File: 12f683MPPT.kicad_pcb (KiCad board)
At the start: 2 copper layers, 97.8 x 72.6 mm, 58 parts, among them J1(+) Conn_01x01_Male, J2(-) Conn_01x01_Male, J3(-) Conn_01x01_Male, J4(+) Conn_01x01_Male, J5(Vin) Vin, J6(GND) GND, J7(12V) 12V, Q1(BUK9511-55A) BUK9511-55A127, Q2(BUK9511-55A) BUK9511-55A127, Q3(2N2222A) 2N2222A, Q4(2N2222A) 2N2222A, Q5(2N2907A) 2N2907A, SW1 SW_Push

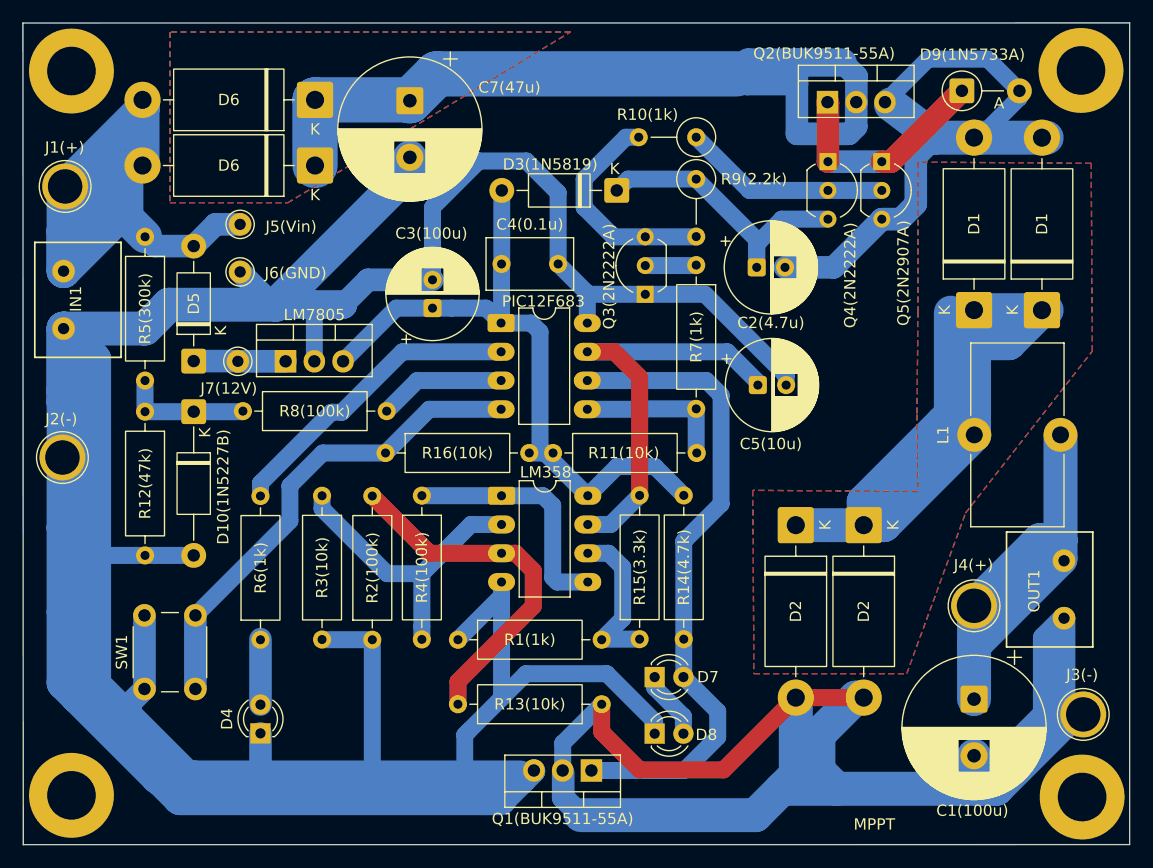
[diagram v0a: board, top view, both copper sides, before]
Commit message: Hints on the capacity of the bootstrap capacitor C2.
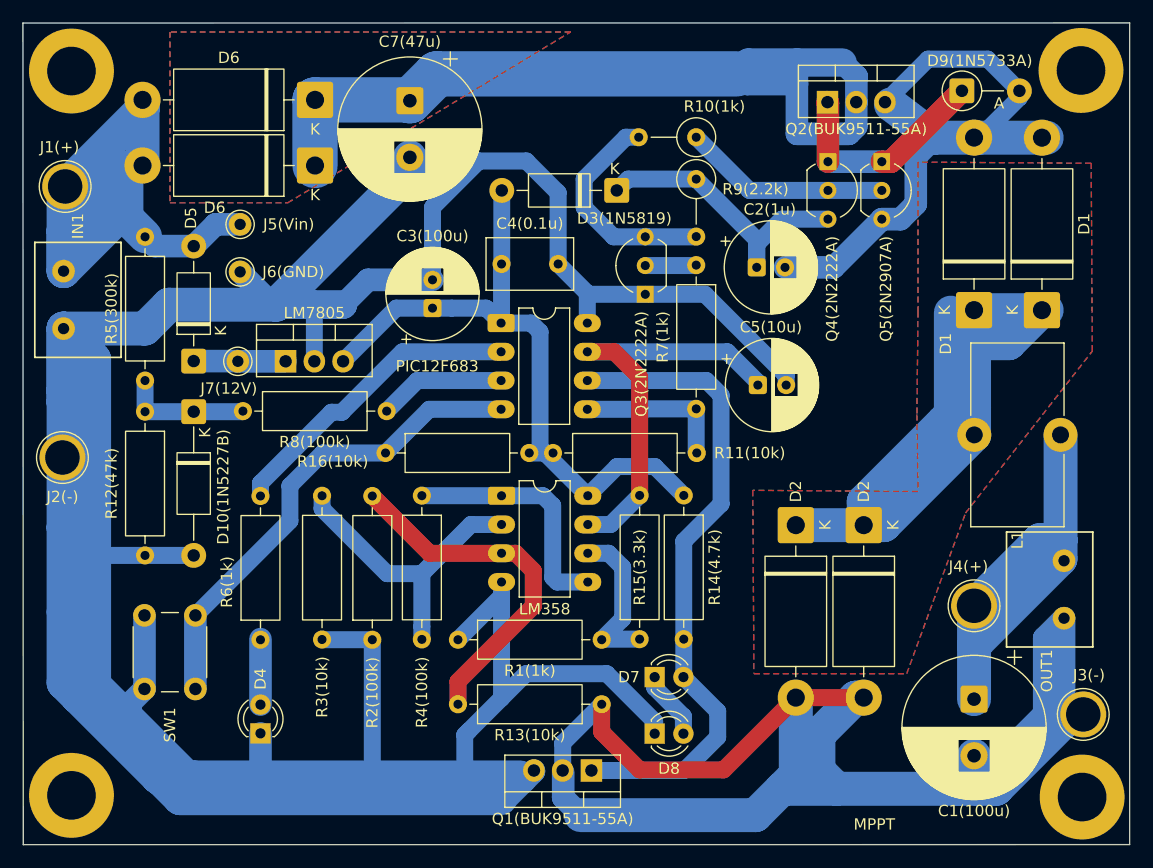
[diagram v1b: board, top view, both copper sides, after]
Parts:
- renumbered C2(4.7u) to C2(1u)
